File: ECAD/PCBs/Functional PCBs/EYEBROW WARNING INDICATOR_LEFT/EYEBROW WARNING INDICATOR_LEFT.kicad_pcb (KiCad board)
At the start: 2 copper layers, 96.1 x 78.8 mm, 43 parts, among them J1 BL IN, J2 BL OUT, J3 SW, SW1 FIRE, SW2 MC/APU FIRE

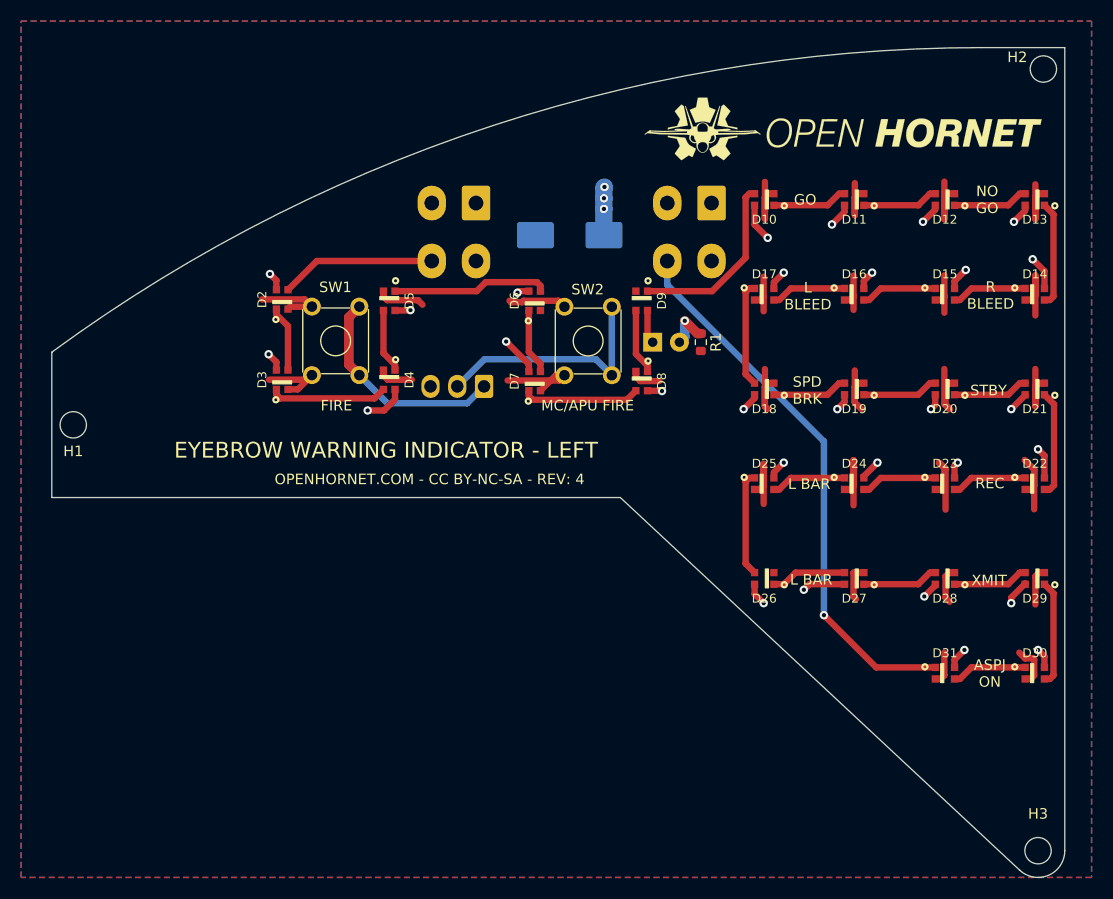
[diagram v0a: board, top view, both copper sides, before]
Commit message: #1159 - Reverse orientation of Status LED
Reversed orientation of D1 status LED
Moved R1 to correct side of D1
Assigned JLC PN to R1
Updated R1 value to 120ohm
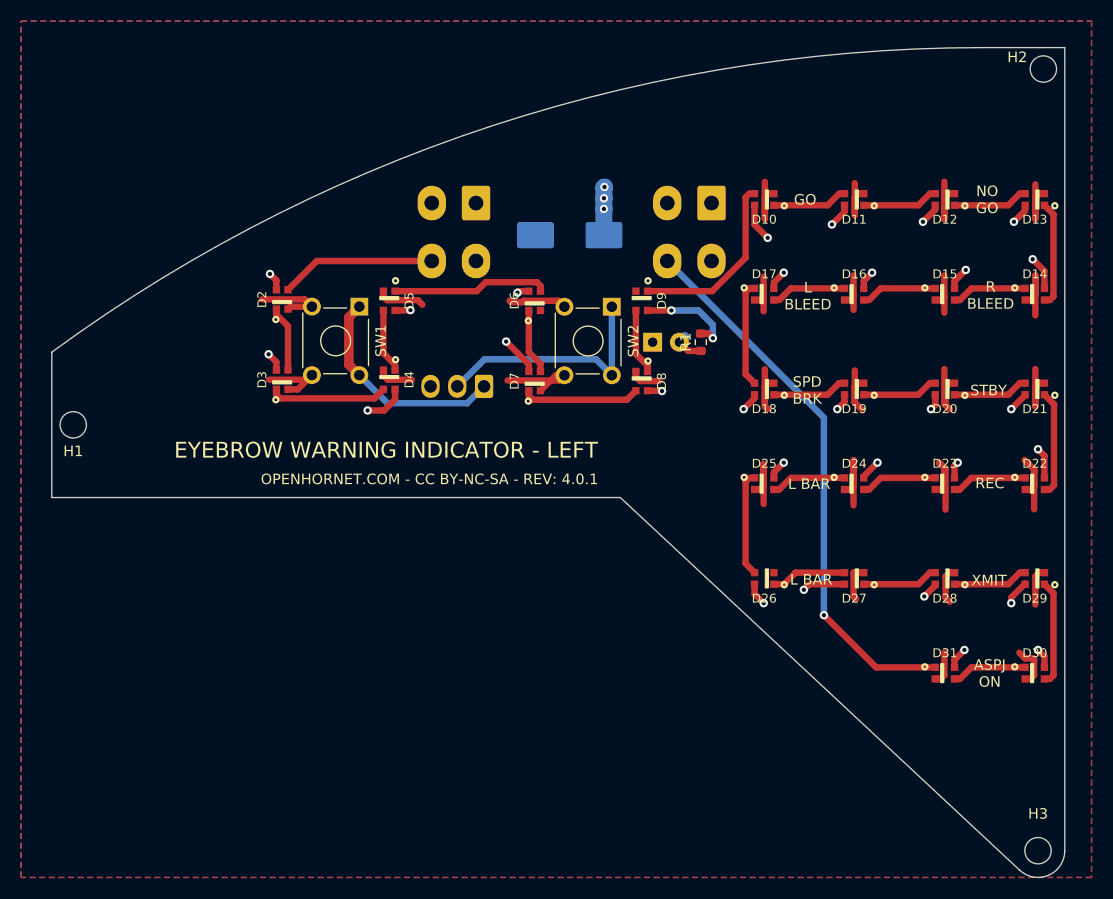
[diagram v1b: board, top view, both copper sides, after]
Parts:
- removed G***: LOGO, KiCAD Libraries:OH_LOGO_37.7mm_5.9mm
- removed G***: LOGO, KiCAD Libraries:OH_LOGO_ONLY_22mm_12mm
- C1: footprint OH_Footprints:CP_Elec_8x10 -> Capacitor_SMD:CP_Elec_8x10
- D1: footprint OH_Footprints:LED_D3.0mm -> LED_THT:LED_D3.0mm
- J1, J2: footprint OH_Footprints:Molex_Mini-Fit_Jr_5566-04A_2x02_P4.20mm_Vertical -> Connector_Molex:Molex_Mini-Fit_Jr_5566-04A_2x02_P4.20mm_Vertical
- J3: footprint OH_Footprints:Molex_KK-254_AE-6410-03A_1x03_P2.54mm_Vertical -> Connector_Molex:Molex_KK-254_AE-6410-03A_1x03_P2.54mm_Vertical
- R1: value R -> 120; footprint OH_Footprints:R_0603_1608Metric -> Resistor_SMD:R_0603_1608Metric
- SW1, SW2: footprint OH_Footprints:SW_TH_Tactile_Omron_B3F-10xx -> Button_Switch_THT:SW_TH_Tactile_Omron_B3F-10xx
- turned R1 to 90 degrees
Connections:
- D1 pad 1: +5V -> GND
- R1 pad 2: GND -> +5V
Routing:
- net +5V: track 67.1 -> 73.3 mm, vias 29 -> 31
- net /MC_SW: track 22.9 -> 28.4 mm
- net GND: track 165.0 -> 160.1 mm
- net Net-(D1-A): track 4.27 -> 3.09 mm, vias 1 -> 0
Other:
- board text added: "OPENHORNET.COM - CC BY-NC-SA - REV: 4.0.1"
- board text removed: "OPENHORNET.COM - CC BY-NC-SA - REV: 4"
